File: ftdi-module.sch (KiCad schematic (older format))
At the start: 48 parts, among them J1 WE_629105150521, U1 FT2232HL-REEL, Y1 KX-7_12,MHz

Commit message: Remove power diodes
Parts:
- removed D? (x2): PMEG3005EH, Diode_SMD:D_SOD-123F, symbol Diode:PMEG3005EH
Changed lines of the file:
@@
 VCC12V0
-$Comp
-L Diode:PMEG3005EH D?
-U 1 1 6245583F
-P 10250 5000
-F 0 "D?" H 10250 5100 50  0000 C CNN
-F 1 "PMEG3005EH" H 10200 4900 50  0000 C CNN
-F 2 "Diode_SMD:D_SOD-123F" H 10250 4825 50  0001 C CNN
-F 3 "https://assets.nexperia.com/documents/data-sheet/PMEGXX05EH_EJ_SER.pdf" H 10250 5000 50  0001 C CNN
-	1    10250 5000
-	-1   0    0    1
-$EndComp
-$Comp
-L Diode:PMEG3005EH D?
-U 1 1 624568EB
-P 10250 5300
-F 0 "D?" H 10250 5200 50  0000 C CNN
-F 1 "PMEG3005EH" H 10200 5400 50  0000 C CNN
-F 2 "Diode_SMD:D_SOD-123F" H 10250 5125 50  0001 C CNN
-F 3 "https://assets.nexperia.com/documents/data-sheet/PMEGXX05EH_EJ_SER.pdf" H 10250 5300 50  0001 C CNN
-	1    10250 5300
-	-1   0    0    1
-$EndComp
 $Comp
 L antmicroDCDCConverters:AP62301WU-7 U?

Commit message: Schematic complete
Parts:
- removed S1: MSS3-V-T_R, antmicro-footprints:Switch_Slide_MSS3, symbol antmicroSlideSwitches:MSS3-V-T_R
- added D3, D4: MBRS330T3G, antmicro-footprints:MBRS340T3, symbol antmicroDiodesRectifiersSingle:MBRS330T3G
- gave numbers to parts that had none: 10
- renumbered 5V_USB to 5V_USB1, SCL to SCL1, SDA to SDA1
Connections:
- net labels removed: 3V3_EN
- wire segments 169 -> 164
- no-connect marks 5 -> 6
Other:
- note removed: "EN floating for \nauto startup\n"
- note removed: "Power Switch\n"
- moved on the sheet: 3V3, 5V0, 5V_USB1, D2, R7, SCL1, SDA1

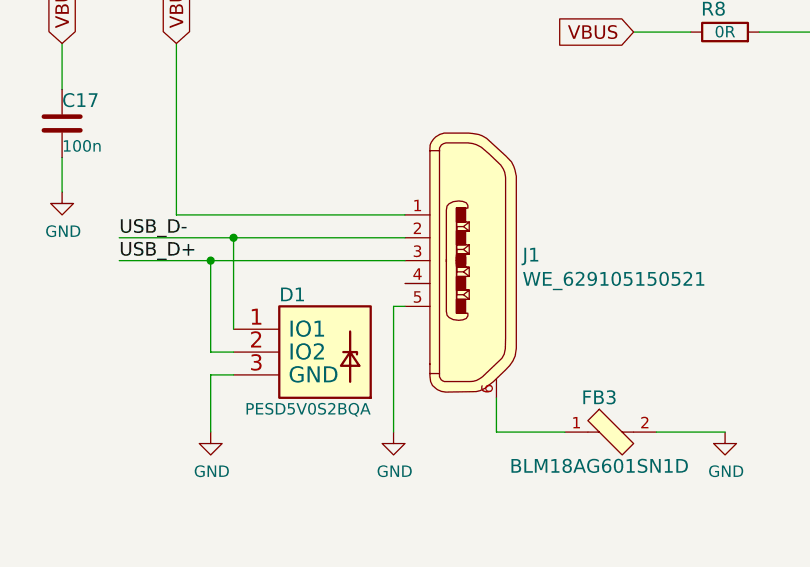
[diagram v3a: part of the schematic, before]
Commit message: Initial component placement done
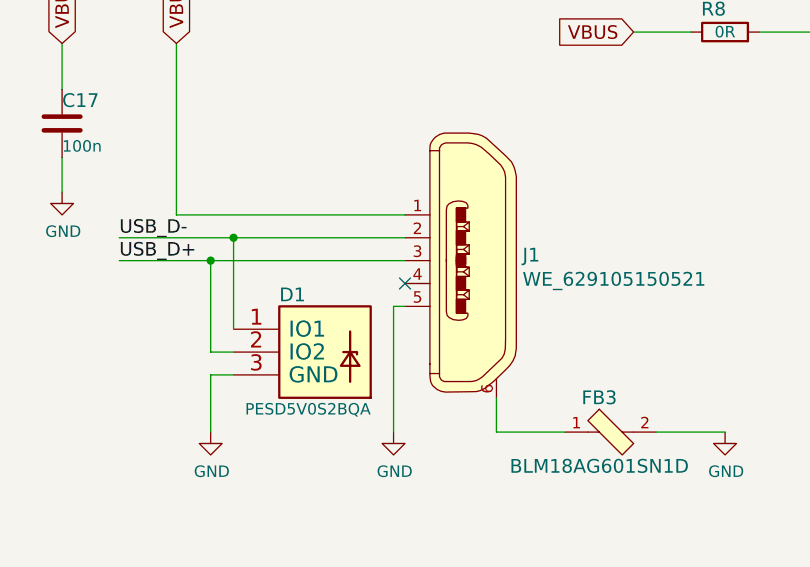
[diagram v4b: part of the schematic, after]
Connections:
- no-connect marks 6 -> 7
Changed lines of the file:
@@
 	1    0    0    -1
 $EndComp
+NoConn ~ 12250 2750
 $EndSCHEMATC

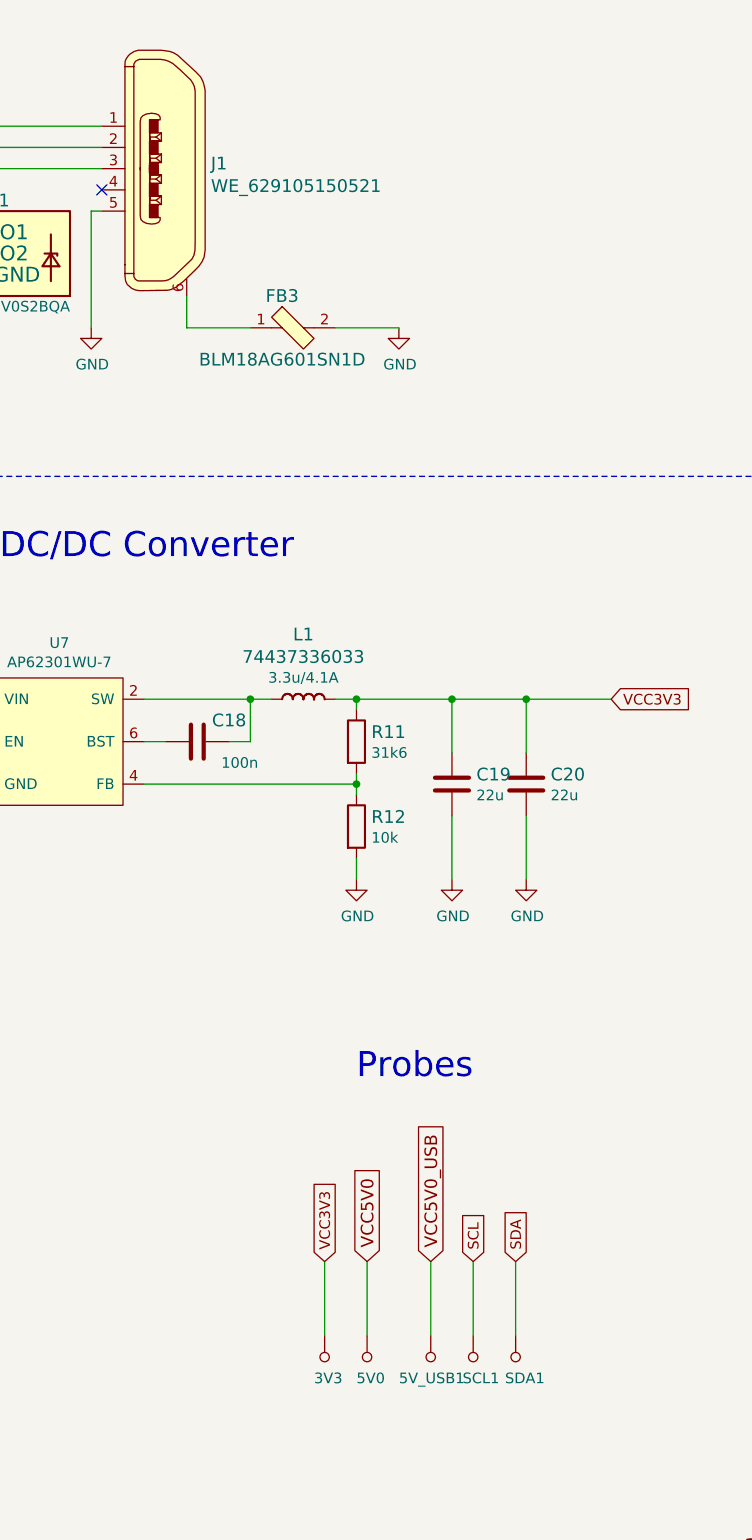
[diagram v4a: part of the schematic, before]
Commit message: Initial routing. Small schematics improvements
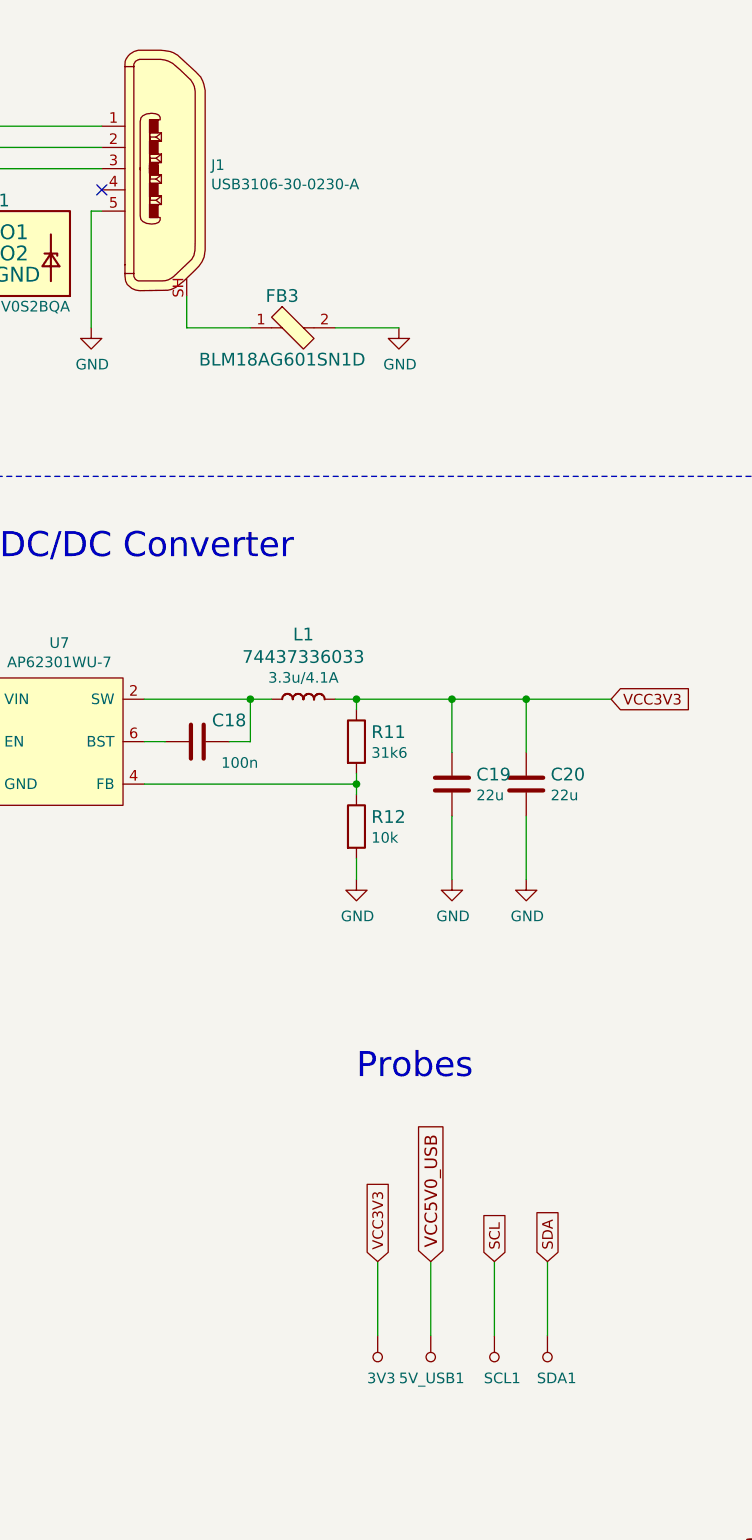
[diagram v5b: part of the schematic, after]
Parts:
- removed 5V0: TP_SMD1MM, antmicro-footprints:Testpoint_smd_1mm, symbol antmicroTestPoints:TP_SMD1MM
- removed J1: WE_629105150521, antmicro-footprints:USB_Micro_B_Female_629105150521, symbol antmicroUSBDVIHDMIConnectors:WE_629105150521
- added J1: USB3106-30-0230-A, antmicro-footprints:usb3106-30-0230, symbol antmicroUSBDVIHDMIConnectors:USB3106-30-0230-A
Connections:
- net GND: now also J1.5
- net USB_D+: now also J1.3
- net USB_D-: now also J1.2
- net VBUS: now also J1.1
- net at FB3.1: now also J1.SH
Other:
- moved on the sheet: 3V3, SCL1, SDA1
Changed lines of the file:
@@
 NoConn ~ 3400 3150
 $Comp
-L antmicroUSBDVIHDMIConnectors:WE_629105150521 J1
-U 1 1 62332491
-P 12550 2650
-F 0 "J1" H 12336 2674 60  0000 R CNN
-F 1 "WE_629105150521" H 12336 2568 60  0000 R CNN
-F 2 "antmicro-footprints:USB_Micro_B_Female_629105150521" H 12750 2850 60  0001 L CNN
-F 3 "" H 12750 2950 60  0001 L CNN
-F 4 "629105150521" H 12750 3150 60  0001 L CNN "MPN"
-F 5 "Wurth_Elektronik" H 12750 3750 60  0001 L CNN "Manufacturer"
-	1    12550 2650
-	-1   0    0    -1
-$EndComp
-$Comp
 L antmicroResistors0603:R_0R_0603 R8
 U 1 1 62334395
@@
 Text Notes 13450 6950 0    118  ~ 0
 Probes
-Text GLabel 13300 7800 1    50   Input ~ 0
+Text GLabel 13550 7800 1    50   Input ~ 0
 VCC3V3
 $Comp
 L antmicroTestPoints:TP_SMD1MM 3V3
 U 1 1 6248DEA2
-P 13300 8250
-F 0 "3V3" H 13250 8150 50  0000 L CNN
-F 1 "TP_SMD1MM" H 13300 8150 50  0001 C CNN
-F 2 "antmicro-footprints:Testpoint_smd_1mm" H 13500 8450 60  0001 L CNN
-F 3 "" H 13500 8550 60  0001 L CNN
-	1    13300 8250
-	1    0    0    -1
-$EndComp
-$Comp
-L antmicroTestPoints:TP_SMD1MM 5V0
-U 1 1 6248E47B
-P 13500 8250
-F 0 "5V0" H 13450 8150 50  0000 L CNN
-F 1 "TP_SMD1MM" H 13500 8150 50  0001 C CNN
-F 2 "antmicro-footprints:Testpoint_smd_1mm" H 13700 8450 60  0001 L CNN
-F 3 "" H 13700 8550 60  0001 L CNN
-	1    13500 8250
+P 13550 8250
+F 0 "3V3" H 13500 8150 50  0000 L CNN
+F 1 "TP_SMD1MM" H 13550 8150 50  0001 C CNN
+F 2 "antmicro-footprints:Testpoint_smd_1mm" H 13750 8450 60  0001 L CNN
+F 3 "" H 13750 8550 60  0001 L CNN
+	1    13550 8250
 	1    0    0    -1
 $EndComp
 Wire Wire Line
-	13300 8150 13300 7800
-Wire Wire Line
-	13500 8150 13500 7800
+	13550 8150 13550 7800
 Text GLabel 5150 7350 0    50   Input ~ 0
 1V8_FT
@@
 Text Label 2950 2850 0    59   ~ 0
 USB_D+
-Text GLabel 13500 7800 1    59   Input ~ 0
-VCC5V0
 $Comp
 L antmicroTestPoints:TP_SMD1MM SCL1
 U 1 1 628ECDC0
-P 14000 8250
-F 0 "SCL1" H 13950 8150 50  0000 L CNN
-F 1 "TP_SMD1MM" H 14000 8150 50  0001 C CNN
-F 2 "antmicro-footprints:Testpoint_smd_1mm" H 14200 8450 60  0001 L CNN
-F 3 "" H 14200 8550 60  0001 L CNN
-	1    14000 8250
+P 14100 8250
+F 0 "SCL1" H 14050 8150 50  0000 L CNN
+F 1 "TP_SMD1MM" H 14100 8150 50  0001 C CNN
+F 2 "antmicro-footprints:Testpoint_smd_1mm" H 14300 8450 60  0001 L CNN
+F 3 "" H 14300 8550 60  0001 L CNN
+	1    14100 8250
 	1    0    0    -1
 $EndComp
-Text GLabel 14000 7800 1    50   Input ~ 0
+Text GLabel 14100 7800 1    50   Input ~ 0
 SCL
-Text GLabel 14200 7800 1    50   Input ~ 0
+Text GLabel 14350 7800 1    50   Input ~ 0
 SDA
 $Comp
 L antmicroTestPoints:TP_SMD1MM SDA1
 U 1 1 6295A452
-P 14200 8250
-F 0 "SDA1" H 14150 8150 50  0000 L CNN
-F 1 "TP_SMD1MM" H 14200 8150 50  0001 C CNN
-F 2 "antmicro-footprints:Testpoint_smd_1mm" H 14400 8450 60  0001 L CNN
-F 3 "" H 14400 8550 60  0001 L CNN
-	1    14200 8250
+P 14350 8250
+F 0 "SDA1" H 14300 8150 50  0000 L CNN
+F 1 "TP_SMD1MM" H 14350 8150 50  0001 C CNN
+F 2 "antmicro-footprints:Testpoint_smd_1mm" H 14550 8450 60  0001 L CNN
+F 3 "" H 14550 8550 60  0001 L CNN
+	1    14350 8250
 	1    0    0    -1
 $EndComp
 Wire Wire Line
-	14000 7800 14000 8150
+	14100 7800 14100 8150
 Wire Wire Line
-	14200 7800 14200 8150
+	14350 7800 14350 8150
 Text Notes 11400 4500 0    118  ~ 0
 3V3 DC/DC Converter
@@
 $EndComp
 NoConn ~ 12250 2750
+$Comp
+L antmicroUSBDVIHDMIConnectors:USB3106-30-0230-A J1
+U 1 1 624C6E54
+P 12550 2650
+F 0 "J1" H 12335 2667 50  0000 R CNN
+F 1 "USB3106-30-0230-A" H 12335 2576 50  0000 R CNN
+F 2 "antmicro-footprints:usb3106-30-0230" H 12750 2850 60  0001 L CNN
+F 3 "https://gct.co/files/drawings/usb3106.pdf" H 12750 2950 60  0001 L CNN
+F 4 "USB3106-30-0230-A" H 12750 3150 60  0001 L CNN "MPN"
+F 5 "Molex" H 12750 3750 60  0001 L CNN "Manufacturer"
+	1    12550 2650
+	-1   0    0    -1
+$EndComp
 $EndSCHEMATC

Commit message: First revision of PCB finished
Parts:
- added R36, R37: R_4k7_0402, antmicro-footprints:0402-res, symbol antmicroResistors0402:R_4k7_0402
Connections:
- net SCL: now also R36.2
- net SDA: now also R37.2
- net VCC3V3: now also R36.1, R37.1
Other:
- note added: "I2C Pull-Ups"
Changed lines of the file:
@@
 	-1   0    0    -1
 $EndComp
+$Comp
+L antmicroResistors0402:R_4k7_0402 R36
+U 1 1 6251E28E
+P 7900 5450
+F 0 "R36" V 7855 5520 60  0000 L CNN
+F 1 "R_4k7_0402" H 7900 5300 60  0001 C CNN
+F 2 "antmicro-footprints:0402-res" H 8100 5650 60  0001 L CNN
+F 3 "" H 7900 5450 50  0001 C CNN
+F 4 "VISHAY" H 8100 5850 60  0001 L CNN "Manufacturer"
+F 5 "MCS04020C4701FE000" H 8100 5750 60  0001 L CNN "MPN"
+F 6 "4k7" V 7953 5520 50  0000 L CNN "Val"
+	1    7900 5450
+	0    1    1    0
+$EndComp
+$Comp
+L antmicroResistors0402:R_4k7_0402 R37
+U 1 1 6251FE62
+P 8200 5450
+F 0 "R37" V 8155 5520 60  0000 L CNN
+F 1 "R_4k7_0402" H 8200 5300 60  0001 C CNN
+F 2 "antmicro-footprints:0402-res" H 8400 5650 60  0001 L CNN
+F 3 "" H 8200 5450 50  0001 C CNN
+F 4 "VISHAY" H 8400 5850 60  0001 L CNN "Manufacturer"
+F 5 "MCS04020C4701FE000" H 8400 5750 60  0001 L CNN "MPN"
+F 6 "4k7" V 8253 5520 50  0000 L CNN "Val"
+	1    8200 5450
+	0    1    1    0
+$EndComp
+Text GLabel 7900 5050 1    50   Input ~ 0
+VCC3V3
+Text GLabel 8200 5050 1    50   Input ~ 0
+VCC3V3
+Wire Wire Line
+	7900 5300 7900 5050
+Wire Wire Line
+	8200 5300 8200 5050
+Text GLabel 7700 5800 0    50   Input ~ 0
+SCL
+Text GLabel 7700 6000 0    50   Input ~ 0
+SDA
+Wire Wire Line
+	7700 5800 7900 5800
+Wire Wire Line
+	7900 5800 7900 5600
+Wire Wire Line
+	7700 6000 8200 6000
+Wire Wire Line
+	8200 6000 8200 5600
+Text Notes 7700 4600 0    79   ~ 0
+I2C Pull-Ups
 $EndSCHEMATC

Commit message: Loclib update
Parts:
- 3V3, 5V_USB1, SCL1, SDA1: footprint antmicro-footprints:Testpoint_smd_1mm -> nuc-compute-cluster-power-breakout-footprints:Testpoint_smd_1mm; symbol antmicroTestPoints:TP_SMD1MM -> nuc-compute-cluster-power-breakout:TP_SMD1MM
- C1, C2: footprint antmicro-footprints:0402-cap -> nuc-compute-cluster-power-breakout-footprints:0402-cap; symbol antmicroCapacitors0402:C_27p_0402 -> nuc-compute-cluster-power-breakout:C_27p_0402
- C10, C11, C12, C17, C18, C3, C4, C5, C6, C7, C8, C9: footprint antmicro-footprints:0402-cap -> nuc-compute-cluster-power-breakout-footprints:0402-cap; symbol antmicroCapacitors0402:C_100n_0402 -> nuc-compute-cluster-power-breakout:C_100n_0402
- C13: footprint antmicro-footprints:0402-cap -> nuc-compute-cluster-power-breakout-footprints:0402-cap; symbol antmicroCapacitors0402:C_3u3_0402 -> nuc-compute-cluster-power-breakout:C_3u3_0402
- C14, C15: footprint antmicro-footprints:0402-cap -> nuc-compute-cluster-power-breakout-footprints:0402-cap; symbol antmicroCapacitors0402:C_4n7_0402 -> nuc-compute-cluster-power-breakout:C_4n7_0402
- C16: footprint antmicro-footprints:0603-cap -> nuc-compute-cluster-power-breakout-footprints:0603-cap; symbol antmicroCapacitors0603:C_10u_16V_0603 -> nuc-compute-cluster-power-breakout:C_10u_16V_0603
- C19, C20: footprint antmicro-footprints:0603-cap -> nuc-compute-cluster-power-breakout-footprints:0603-cap; symbol antmicroCapacitors0603:C_22u_0603 -> nuc-compute-cluster-power-breakout:C_22u_0603
- D1: footprint antmicro-footprints:TPD2E009DRTR -> nuc-compute-cluster-power-breakout-footprints:TPD2E009DRTR; symbol antmicroTVSDiodes:PESD5V0S2BQA -> nuc-compute-cluster-power-breakout:PESD5V0S2BQA
- D2: footprint antmicro-footprints:LED_0603 -> nuc-compute-cluster-power-breakout-footprints:LED_0603; symbol antmicroLEDIndicationDiscrete:KP-1608CGCK -> nuc-compute-cluster-power-breakout:KP-1608CGCK
- D3, D4: footprint antmicro-footprints:MBRS340T3 -> nuc-compute-cluster-power-breakout-footprints:MBRS340T3; symbol antmicroDiodesRectifiersSingle:MBRS330T3G -> nuc-compute-cluster-power-breakout:MBRS330T3G
- FB1, FB2, FB3: footprint antmicro-footprints:0603 -> nuc-compute-cluster-power-breakout-footprints:0603; symbol antmicroFerriteBeadsandChips:BLM18AG601SN1D -> nuc-compute-cluster-power-breakout:BLM18AG601SN1D
- J1: footprint antmicro-footprints:usb3106-30-0230 -> nuc-compute-cluster-power-breakout-footprints:usb3106-30-0230; symbol antmicroUSBDVIHDMIConnectors:USB3106-30-0230-A -> nuc-compute-cluster-power-breakout:USB3106-30-0230-A
- L1: footprint antmicro-footprints:WE_74437336033 -> nuc-compute-cluster-power-breakout-footprints:WE_74437336033; symbol antmicroFixedInductors:74437336033 -> nuc-compute-cluster-power-breakout:74437336033
- R1, R36, R37: footprint antmicro-footprints:0402-res -> nuc-compute-cluster-power-breakout-footprints:0402-res; symbol antmicroResistors0402:R_4k7_0402 -> nuc-compute-cluster-power-breakout:R_4k7_0402
- R11: footprint antmicro-footprints:0402-res -> nuc-compute-cluster-power-breakout-footprints:0402-res; symbol antmicroResistors0402:R_31k6_0402 -> nuc-compute-cluster-power-breakout:R_31k6_0402
- R12, R2: footprint antmicro-footprints:0402-res -> nuc-compute-cluster-power-breakout-footprints:0402-res; symbol antmicroResistors0402:R_10k_0402 -> nuc-compute-cluster-power-breakout:R_10k_0402
- R3: footprint antmicro-footprints:0402-res -> nuc-compute-cluster-power-breakout-footprints:0402-res; symbol antmicroResistors0402:R_12k_0402 -> nuc-compute-cluster-power-breakout:R_12k_0402
- R4, R5, R8: footprint antmicro-footprints:0603-res -> nuc-compute-cluster-power-breakout-footprints:0603-res; symbol antmicroResistors0603:R_0R_0603 -> nuc-compute-cluster-power-breakout:R_0R_0603
- R6: footprint antmicro-footprints:0402-res -> nuc-compute-cluster-power-breakout-footprints:0402-res; symbol antmicroResistors0402:R_220R_0402 -> nuc-compute-cluster-power-breakout:R_220R_0402
- R7: footprint antmicro-footprints:0402-res -> nuc-compute-cluster-power-breakout-footprints:0402-res; symbol antmicroResistors0402:R_330R_0402 -> nuc-compute-cluster-power-breakout:R_330R_0402
- U1: footprint antmicro-footprints:LQFP-64_10x10mm -> nuc-compute-cluster-power-breakout-footprints:LQFP-64_10x10mm; symbol antmicroInterfaceControllers:FT2232HL-REEL -> nuc-compute-cluster-power-breakout:FT2232HL-REEL
- U7: footprint antmicro-footprints:TSOT23-6 -> nuc-compute-cluster-power-breakout-footprints:TSOT23-6; symbol antmicroDCDCConverters:AP62301WU-7 -> nuc-compute-cluster-power-breakout:AP62301WU-7
- Y1: footprint antmicro-footprints:KX-7 -> nuc-compute-cluster-power-breakout-footprints:KX-7; symbol antmicroCrystals:KX-7_12,MHz -> nuc-compute-cluster-power-breakout:KX-7_12,MHz

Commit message: Add remarks on the schematic sheets
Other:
- note added: "REMARK: Missing symbol"
- note added: "TODO: What is the scenario for 5V0 \npower supply without the 12V? \nAdd 0R in the same place as D3 \nand mark D3 and D4 as DNP."
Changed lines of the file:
@@
 U 1 1 624435BD
 P 13900 5550
-F 0 "C19" H 14015 5595 60  0000 L CNN
+F 0 "C19" H 13925 5650 60  0000 L CNN
 F 1 "C_22u_0603" H 13900 5400 60  0001 C CNN
 F 2 "nuc-compute-cluster-power-breakout-footprints:0603-cap" H 14100 5750 60  0001 L CNN
@@
 U 1 1 6244466C
 P 14250 5550
-F 0 "C20" H 14365 5595 60  0000 L CNN
+F 0 "C20" H 14300 5650 60  0000 L CNN
 F 1 "C_22u_0603" H 14250 5400 60  0001 C CNN
 F 2 "nuc-compute-cluster-power-breakout-footprints:0603-cap" H 14450 5750 60  0001 L CNN
@@
 Text Notes 7700 4600 0    79   ~ 0
 I2C Pull-Ups
+Text Notes 14250 9175 0    79   ~ 0
+REMARK: Missing symbol
+Text Notes 9000 4650 0    79   ~ 0
+TODO: What is the scenario for 5V0 \npower supply without the 12V? \nAdd 0R in the same place as D3 \nand mark D3 and D4 as DNP.
 $EndSCHEMATC
